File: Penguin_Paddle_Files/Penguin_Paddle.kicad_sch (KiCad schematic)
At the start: 15 parts, among them J1 Conn_01x01_Socket, J2 AudioPlug3, J3 Conn_01x01_Socket, Q1 NPN, SW1 SW_SPST, SW2 SW_SPST, U1 XIAO-ESP32-S3-DIP

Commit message: Cleaned folders (frogot to commit this a few days ago)
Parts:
- added J4, J5: Conn_01x01_Socket, Connector_Wire:SolderWire-0.1sqmm_1x01_D0.4mm_OD1mm, symbol Connector:Conn_01x01_Socket
- added TP3, TP4: TestPoint, Custom:Copper Pad, symbol Connector:TestPoint
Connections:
- new net: J5.1 (Pin_1), TP4.1
- new net: J4.1 (Pin_1), TP3.1

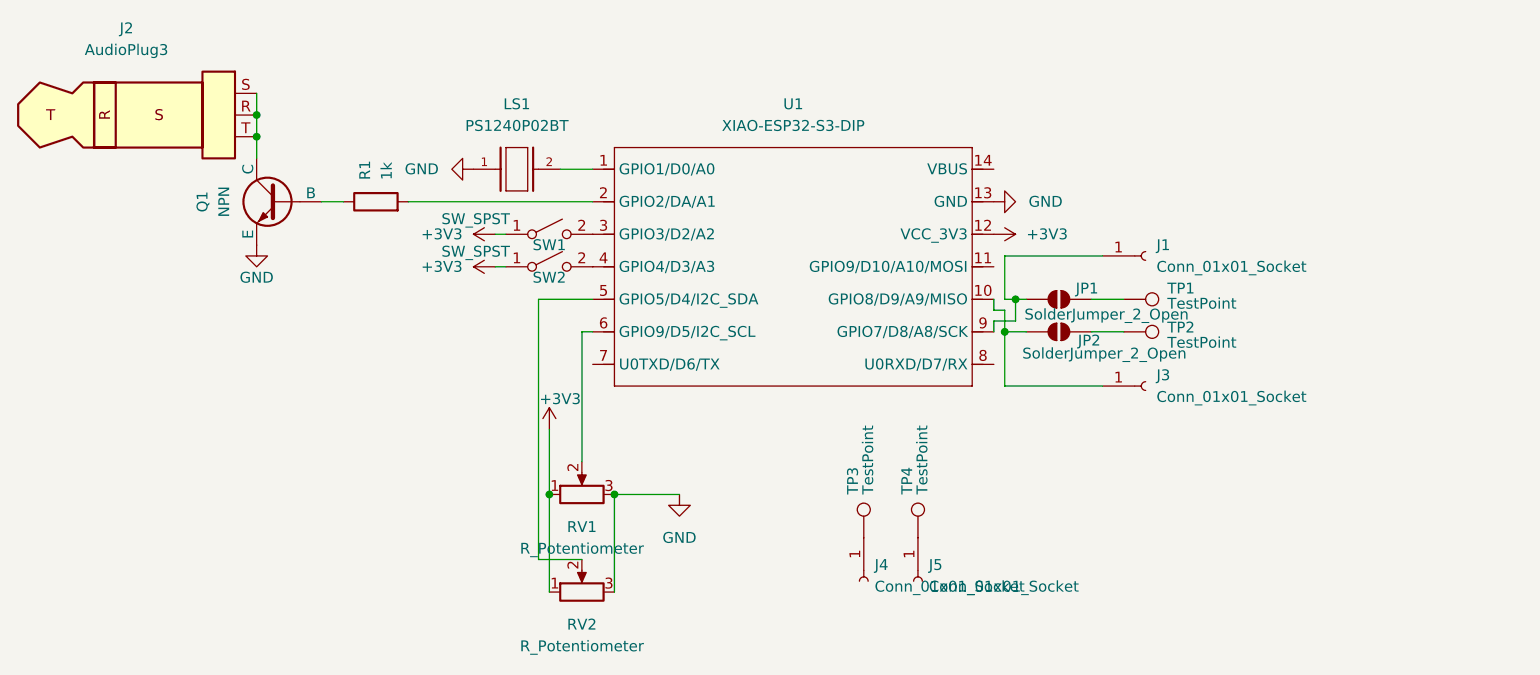
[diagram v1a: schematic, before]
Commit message: Finished Code, Switched to Mircopython, updated Gerbers
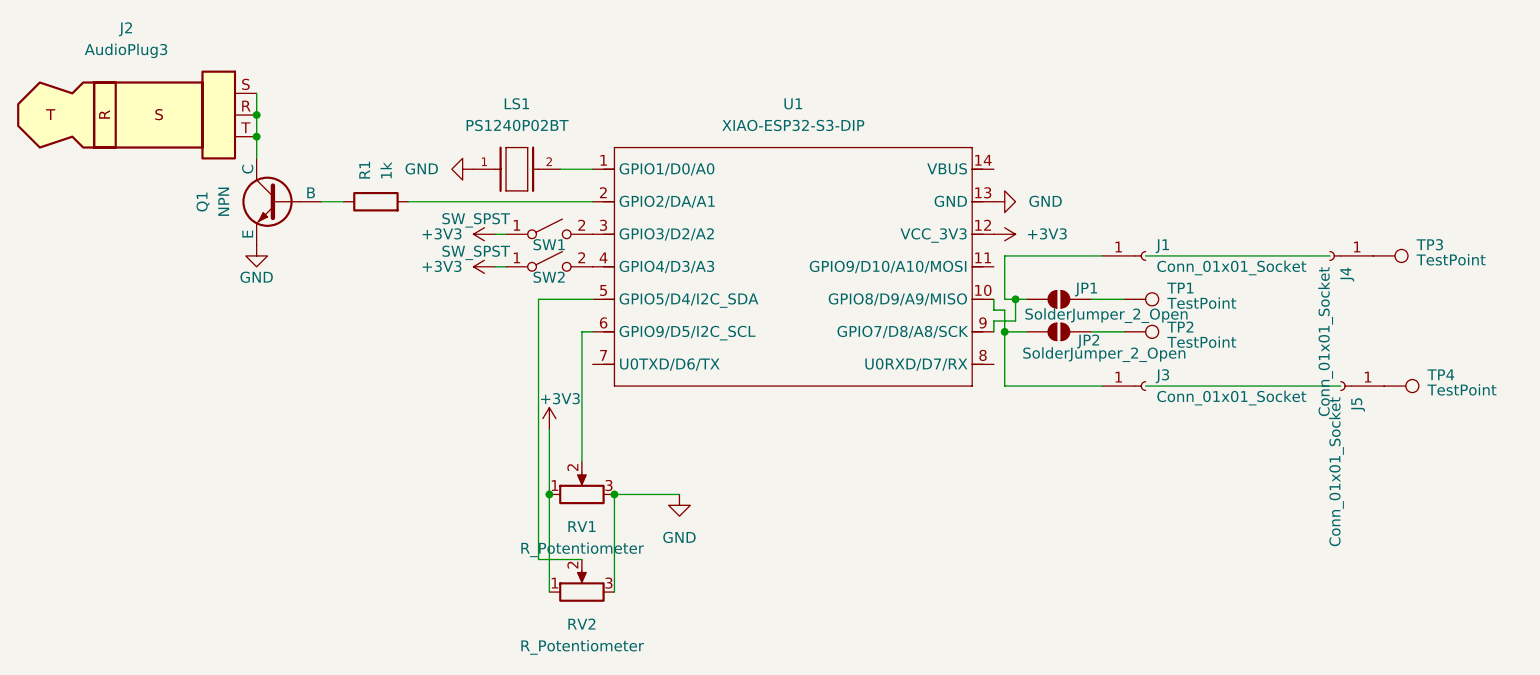
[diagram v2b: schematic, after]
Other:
- moved on the sheet: J4, J5, TP3, TP4
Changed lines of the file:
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@@
+	(wire
+		(pts
+			(xy 203.2 87.63) (xy 224.79 87.63)
+		)
+		(stroke
+			(width 0)
+			(type default)
+		)
+	)
 	(wire
 		(pts
@@
 	(wire
 		(pts
+			(xy 203.2 102.87) (xy 226.06 102.87)
+		)
+		(stroke
+			(width 0)
+			(type default)
+		)
+	)
+	(wire
+		(pts
 			(xy 186.69 93.98) (xy 186.69 96.52)
 		)
@@
 	(symbol
 		(lib_id "Connector:TestPoint")
-		(at 176.53 120.65 0)
+		(at 231.14 102.87 270)
 		(unit 1)
 		(exclude_from_sim no)
@@
 		(dnp no)
 		(property "Reference" "TP4"
-			(at 175.2599 115.57 90)
+			(at 236.22 101.5999 90)
 			(effects
 				(font
@@
 		)
 		(property "Value" "TestPoint"
-			(at 177.038 115.57 90)
+			(at 236.22 103.378 90)
 			(effects
 				(font
@@
 		)
 		(property "Footprint" "Custom:Copper Pad"
-			(at 181.61 120.65 0)
+			(at 231.14 107.95 0)
 			(effects
 				(font
@@
 		)
 		(property "Datasheet" "~"
-			(at 181.61 120.65 0)
+			(at 231.14 107.95 0)
 			(effects
 				(font
@@
 		)
 		(property "Description" "test point"
-			(at 176.53 120.65 0)
+			(at 231.14 102.87 0)
 			(effects
 				(font
@@
 	(symbol
 		(lib_id "Connector:TestPoint")
-		(at 170.18 120.65 0)
+		(at 229.87 87.63 270)
 		(unit 1)
 		(exclude_from_sim no)
@@
 		(dnp no)
 		(property "Reference" "TP3"
-			(at 168.9099 115.57 90)
+			(at 234.95 86.3599 90)
 			(effects
 				(font
@@
 		)
 		(property "Value" "TestPoint"
-			(at 170.688 115.57 90)
+			(at 234.95 88.138 90)
 			(effects
 				(font
@@
 		)
 		(property "Footprint" "Custom:Copper Pad"
-			(at 175.26 120.65 0)
+			(at 229.87 92.71 0)
 			(effects
 				(font
@@
 		)
 		(property "Datasheet" "~"
-			(at 175.26 120.65 0)
+			(at 229.87 92.71 0)
 			(effects
 				(font
@@
 		)
 		(property "Description" "test point"
-			(at 170.18 120.65 0)
+			(at 229.87 87.63 0)
 			(effects
 				(font
@@
 	(symbol
 		(lib_id "Connector:Conn_01x01_Socket")
-		(at 176.53 125.73 270)
+		(at 226.06 102.87 180)
 		(unit 1)
 		(exclude_from_sim no)
@@
 		(fields_autoplaced yes)
 		(property "Reference" "J5"
-			(at 177.8 123.8249 90)
+			(at 227.9651 104.14 90)
 			(effects
 				(font
@@
 		)
 		(property "Value" "Conn_01x01_Socket"
-			(at 177.8 126.3649 90)
+			(at 225.4251 104.14 90)
 			(effects
 				(font
@@
 		)
 		(property "Footprint" "Connector_Wire:SolderWire-0.1sqmm_1x01_D0.4mm_OD1mm"
-			(at 176.53 125.73 0)
+			(at 226.06 102.87 0)
 			(effects
 				(font
@@
 		)
 		(property "Datasheet" "~"
-			(at 176.53 125.73 0)
+			(at 226.06 102.87 0)
 			(effects
 				(font
@@
 		)
 		(property "Description" "Generic connector, single row, 01x01, script generated"
-			(at 176.53 125.73 0)
+			(at 226.06 102.87 0)
 			(effects
 				(font
@@
 	(symbol
 		(lib_id "Connector:Conn_01x01_Socket")
-		(at 170.18 125.73 270)
+		(at 224.79 87.63 180)
 		(unit 1)
 		(exclude_from_sim no)
@@
 		(fields_autoplaced yes)
 		(property "Reference" "J4"
-			(at 171.45 123.8249 90)
+			(at 226.6951 88.9 90)
 			(effects
 				(font
@@
 		)
 		(property "Value" "Conn_01x01_Socket"
-			(at 171.45 126.3649 90)
+			(at 224.1551 88.9 90)
 			(effects
 				(font
@@
 		)
 		(property "Footprint" "Connector_Wire:SolderWire-0.1sqmm_1x01_D0.4mm_OD1mm"
-			(at 170.18 125.73 0)
+			(at 224.79 87.63 0)
 			(effects
 				(font
@@
 		)
 		(property "Datasheet" "~"
-			(at 170.18 125.73 0)
+			(at 224.79 87.63 0)
 			(effects
 				(font
@@
 		)
 		(property "Description" "Generic connector, single row, 01x01, script generated"
-			(at 170.18 125.73 0)
-			(effects
-				(font
+			(at 224.79 87.63 0)
+			(effects
+				(font
